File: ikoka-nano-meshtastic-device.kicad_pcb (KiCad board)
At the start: 2 copper layers, 40.6 x 40.6 mm, 10 parts, among them J1 JST_2mm_LiPo, J2 JST_2mm_LiPo, J3 Qwiic_RA, U1 Seeed Studio XIAO nRF52840, U2 E22-900M30S

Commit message: Update schematic with LCSC part numbers
Signed-off-by: Andrew Yong <me@ndoo.sg>
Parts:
- ST1, ST2, ST3, ST4: value STAND-OFF -> Standoff
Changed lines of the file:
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@@
       (plot_on_all_layers_selection 0x0000000_00000000)
       (disableapertmacros false)
-      (usegerberextensions false)
-      (usegerberattributes true)
-      (usegerberadvancedattributes true)
-      (creategerberjobfile true)
+      (usegerberextensions true)
+      (usegerberattributes false)
+      (usegerberadvancedattributes false)
+      (creategerberjobfile false)
       (dashed_line_dash_ratio 12.000000)
       (dashed_line_gap_ratio 3.000000)
@@
       (psa4output false)
       (plotreference true)
-      (plotvalue true)
+      (plotvalue false)
       (plotinvisibletext false)
       (sketchpadsonfab false)
-      (subtractmaskfromsilk false)
+      (subtractmaskfromsilk true)
       (outputformat 1)
       (mirror false)
-      (drillshape 1)
+      (drillshape 0)
       (scaleselection 1)
-      (outputdirectory "")
+      (outputdirectory "plots/")
     )
   )
@@
   (footprint "OPL_Capacitor:C1206" (layer "F.Cu")
     (at 138.938 90.932)
+    (property "LCSC" "C77085")
     (property "MPN" "GRM31CR60J107ME39L")
     (property "SKU" "302010183")
@@
   (footprint "SparkFun-Connector:JST_SMD_2.0mm-2" (layer "F.Cu")
     (at 143.51 118.11 180)
+    (property "LCSC" "C295747")
     (property "PROD_ID" "CONN-11443")
     (property "Sheetfile" "ikoka-nano-meshtastic-device.kicad_sch")
@@
   (footprint "SparkFun-Connector:JST_SMD_2.0mm-2" (layer "F.Cu")
     (at 161.29 118.11 180)
+    (property "LCSC" "C295747")
     (property "PROD_ID" "CONN-11443")
     (property "Sheetfile" "ikoka-nano-meshtastic-device.kicad_sch")
@@
     (property "Sheetfile" "ikoka-nano-meshtastic-device.kicad_sch")
     (property "Sheetname" "")
+    (property "dnp" "")
+    (property "exclude_from_bom" "")
     (property "ki_description" "Drill holes for mechanically mounting via screws, standoffs, etc.")
     (property "ki_keywords" "SparkFun #4 screw stand off")
+    (attr exclude_from_bom)
     (fp_text reference "ST3" (at 0 -2.032) (layer "F.Fab")
         (effects (font (size 0.5 0.5) (thickness 0.1)) (justify bottom))
     )
-    (fp_text value "STAND-OFF" (at 0 2.032) (layer "F.Fab")
+    (fp_text value "Standoff" (at 0 2.032) (layer "F.Fab")
         (effects (font (size 0.5 0.5) (thickness 0.1)) (justify top))
     )
@@
     (property "Sheetfile" "ikoka-nano-meshtastic-device.kicad_sch")
     (property "Sheetname" "")
+    (property "dnp" "")
+    (property "exclude_from_bom" "")
     (property "ki_description" "Drill holes for mechanically mounting via screws, standoffs, etc.")
     (property "ki_keywords" "SparkFun #4 screw stand off")
+    (attr exclude_from_bom)
     (fp_text reference "ST1" (at 0 -2.032) (layer "F.Fab")
         (effects (font (size 0.5 0.5) (thickness 0.1)) (justify bottom))
     )
-    (fp_text value "STAND-OFF" (at 0 2.032) (layer "F.Fab")
+    (fp_text value "Standoff" (at 0 2.032) (layer "F.Fab")
         (effects (font (size 0.5 0.5) (thickness 0.1)) (justify top))
     )
@@
     (property "Sheetfile" "ikoka-nano-meshtastic-device.kicad_sch")
     (property "Sheetname" "")
+    (property "dnp" "")
+    (property "exclude_from_bom" "")
     (property "ki_description" "Drill holes for mechanically mounting via screws, standoffs, etc.")
     (property "ki_keywords" "SparkFun #4 screw stand off")
+    (attr exclude_from_bom)
     (fp_text reference "ST2" (at 0 -2.032) (layer "F.Fab")
         (effects (font (size 0.5 0.5) (thickness 0.1)) (justify bottom))
     )
-    (fp_text value "STAND-OFF" (at 0 2.032) (layer "F.Fab")
+    (fp_text value "Standoff" (at 0 2.032) (layer "F.Fab")
         (effects (font (size 0.5 0.5) (thickness 0.1)) (justify top))
     )
@@
     (property "Sheetfile" "ikoka-nano-meshtastic-device.kicad_sch")
     (property "Sheetname" "")
+    (property "dnp" "")
+    (property "exclude_from_bom" "")
     (property "ki_description" "Drill holes for mechanically mounting via screws, standoffs, etc.")
     (property "ki_keywords" "SparkFun #4 screw stand off")
+    (attr exclude_from_bom)
     (fp_text reference "ST4" (at 0 -2.032) (layer "F.Fab")
         (effects (font (size 0.5 0.5) (thickness 0.1)) (justify bottom))
     )
-    (fp_text value "STAND-OFF" (at 0 2.032) (layer "F.Fab")
+    (fp_text value "Standoff" (at 0 2.032) (layer "F.Fab")
         (effects (font (size 0.5 0.5) (thickness 0.1)) (justify top))
     )
@@
   (footprint "Seeed Studio XIAO Series Library:XIAO-nRF52840-Sense-14P-2.54-21X17.8MM" (layer "F.Cu")
     (at 152.4 91.948)
+    (property "LCSC" "C17209540")
     (property "Sheetfile" "ikoka-nano-meshtastic-device.kicad_sch")
     (property "Sheetname" "")
@@
   (footprint "SparkFun-Connector:JST_SMD_1.0mm-4_RA" (layer "F.Cu")
     (at 152.4 116.629)
+    (property "LCSC" "C160404")
     (property "PROD_ID" "CONN-13694")
     (property "Sheetfile" "ikoka-nano-meshtastic-device.kicad_sch")
@@
     (property "Check_prices" "https://www.snapeda.com/parts/E22-900M30S/EBYTE/view-part/?ref=eda")
     (property "Description" "\nSX1262 868/915 MHz 1w SPI LoRa Module\n")
+    (property "LCSC" "C411294")
     (property "MANUFACTURER" "EBYTE")
     (property "MAXIMUM_PACKAGE_HEIGHT" "3.97 mm")

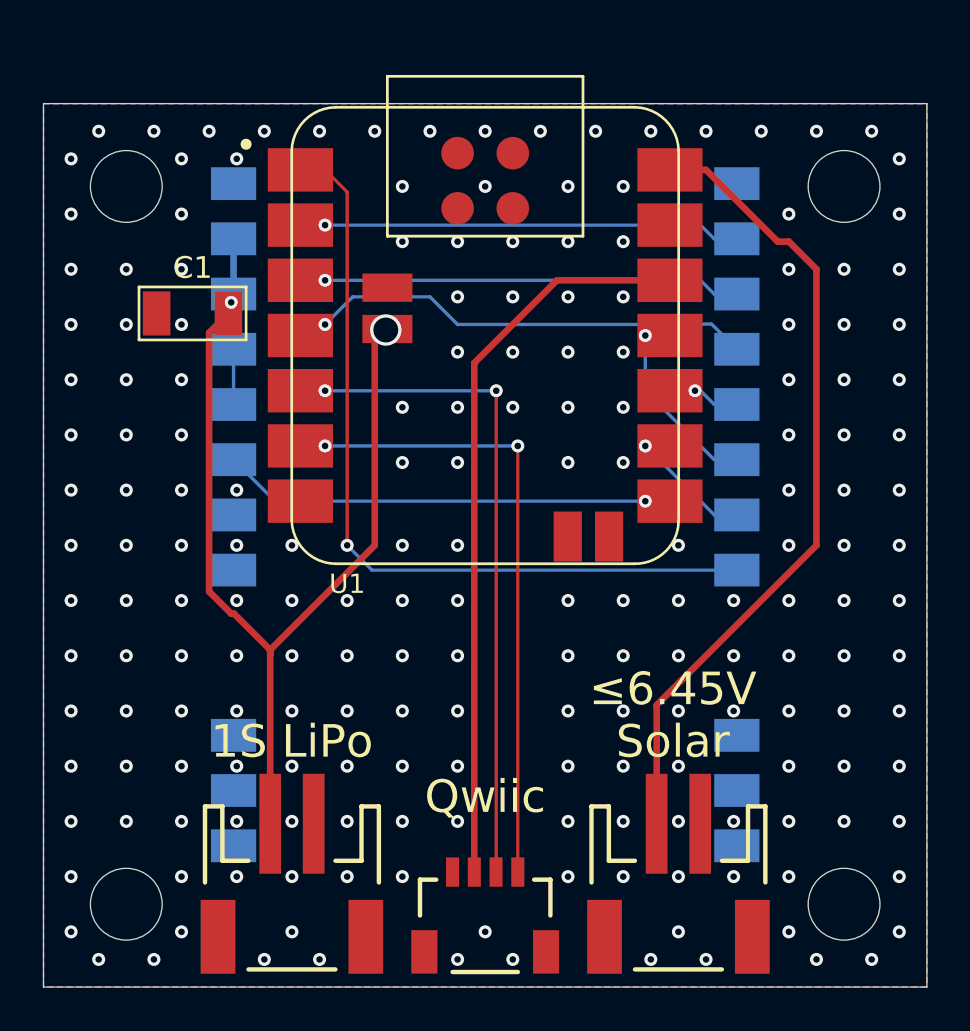
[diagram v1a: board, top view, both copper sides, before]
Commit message: Update ground plane stitching and related generated artifacts; bump PCB revision to 1.1
Signed-off-by: Andrew Yong <me@ndoo.sg>
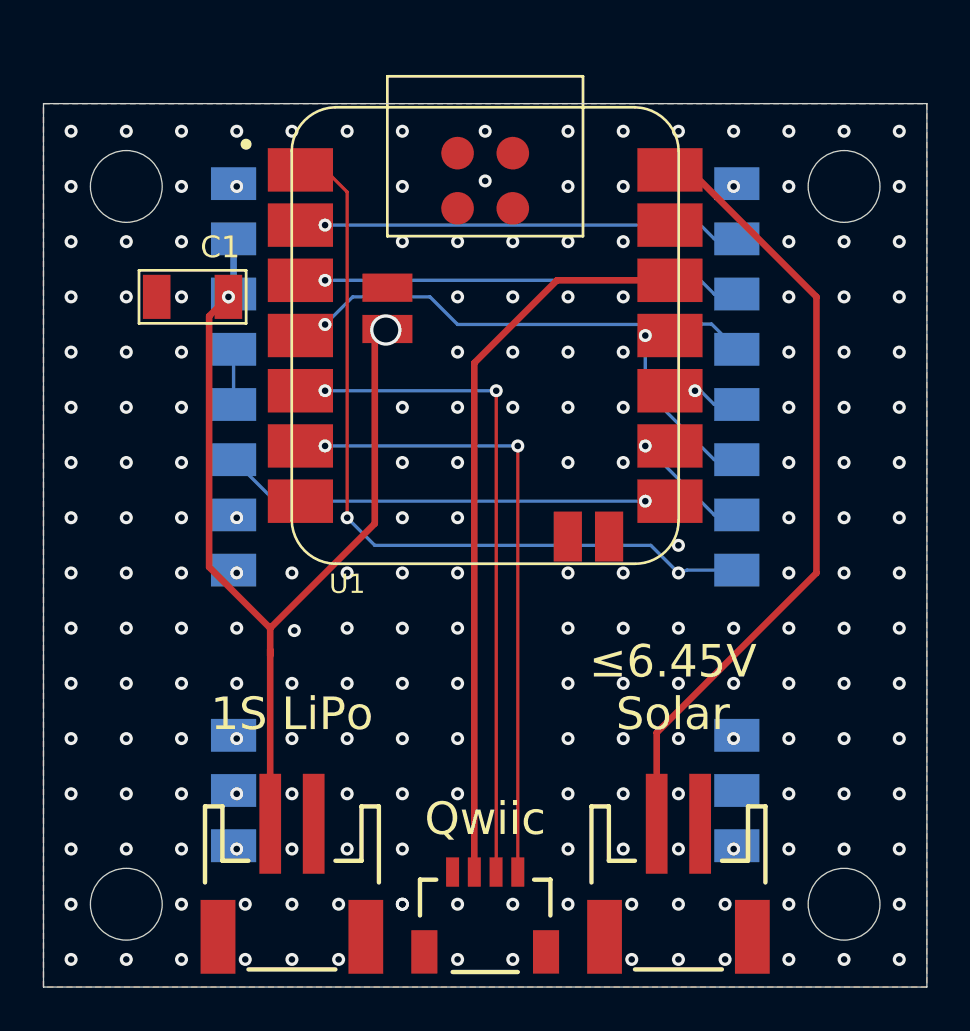
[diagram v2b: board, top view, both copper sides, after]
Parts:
- moved C1 0.76 mm to (138.9, 90.2)
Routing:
- net 5V: track 37.4 -> 36.7 mm
- net SX126X_CS: track 37.2 -> 36.6 mm, vias 1 -> 2
- net GND: vias 194 -> 202

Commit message: Power EBYTE E22 module from 5V and remove JST-PH 2.0 connectors
Power EBYTE E22 module from 5V because VBAT results in very poor transmit power.

Remove JST connectors since the device no longer functions without 5V.

Signed-off-by: Andrew Yong <me@ndoo.sg>
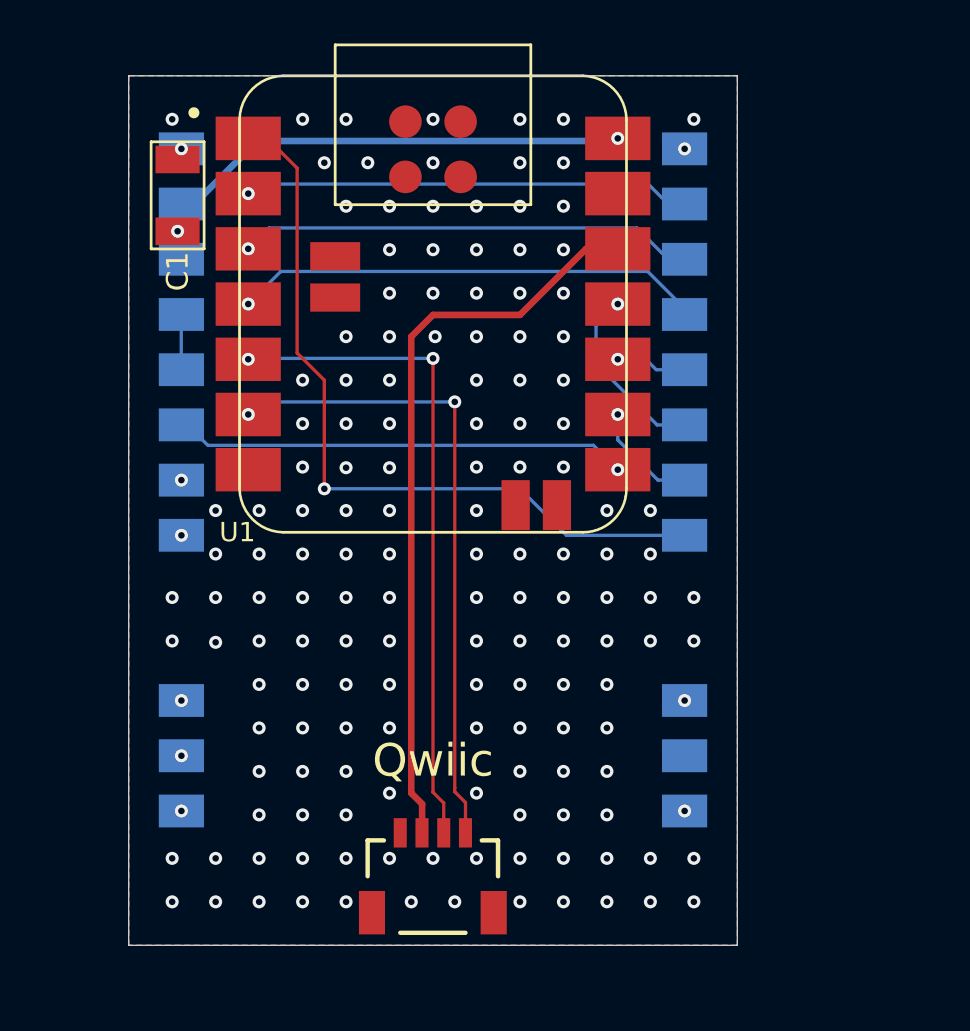
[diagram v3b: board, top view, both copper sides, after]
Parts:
- removed J1, J2: JST_2mm_LiPo, SparkFun-Connector:JST_SMD_2.0mm-2
- removed ST1, ST2, ST3, ST4: Standoff, SparkFun-Hardware:Standoff
- moved C1 4.72 mm to (138.2, 85.5), turned to -90 degrees
- moved J3 3.01 mm to (150.0, 114.8)
- moved U2 2.88 mm to (150.0, 100.0)
- moved U1 2.80 mm to (150.0, 90.5)
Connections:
- C1 pad 2: VBAT -> 5V
- U1 pad 21: GND -> unconnected-(U1-BAT--Pad21)
- U1 pad 22: VBAT -> unconnected-(U1-BAT+-Pad22)
- U2 pad 10: VBAT -> 5V
- U2 pad 9: VBAT -> 5V
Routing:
- net VBAT: track 45.1 -> 0.00 mm, vias 2 -> 0
- net 5V: track 36.7 -> 25.0 mm, vias 0 -> 2
- net SX126X_BUSY: track 19.2 -> 20.9 mm
- net SX126X_RXEN: track 19.7 -> 21.1 mm
- net SX126X_DIO1: track 19.2 -> 20.5 mm
- net SPI_MISO: track 2.18 -> 3.27 mm
- net I2C_SCL: track 28.7 -> 29.8 mm
- net SX126X_CS: track 36.6 -> 35.6 mm, vias 2 -> 1
- net SX126X_RESET: track 20.5 -> 21.4 mm
- net unconnected-(U1-BAT+-Pad22): track 0.00 -> 0.72 mm
- net SPI_SCK: track 5.52 -> 5.01 mm
- net GND: vias 202 -> 158
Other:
- board size 40.6 x 40.6 mm -> 28 x 40 mm
- board text removed: "1S LiPo"
- board text removed: "≤6.45V Solar"
